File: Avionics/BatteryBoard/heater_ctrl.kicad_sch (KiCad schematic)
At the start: 0 parts

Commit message: Added heater control sub-schematic to battery board
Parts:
- added R13: 10k, symbol Device:R_US
- added R14: 31.6k, symbol Device:R_US
- added R15: 1.5k, symbol Device:R_US
- added U10: LMV331, symbol Comparator:LMV331
- added U11, U12: 74AHC1G08, symbol 74xGxx:74AHC1G08
- added U13: 74AHC1G32, symbol 74xGxx:74AHC1G32
- added U14: 74AHC1G04, symbol 74xGxx:74AHC1G04
- added U8: LM4040DBZ-2.5, Package_TO_SOT_SMD:SOT-23, symbol Reference_Voltage:LM4040DBZ-2.5
- added U9: TMP36xS, Package_SO:SOIC-8_3.9x4.9mm_P1.27mm, symbol Sensor_Temperature:TMP36xS
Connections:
- new net: U10.3 (-), U9.1 (V_{OUT})
- new net: R13.1, R14.2, U10.1 (+)
- new net: U12.1, U14.2
- new net: U11.2, U14.4
- new net: R14.1, R15.1, U8.1 (K)
- new net: U10.4, U11.1
- new net: U11.4, U13.1
- new net: U12.4, U13.2
- new net GNDREF: R13.2, U10.2 (V-), U11.3 (GND), U12.3 (GND), U13.3 (GND), U14.3 (GND), U8.2 (A), U9.4 (GND), U9.5 (~{SHUTDOWN})
- new net VCC: R15.2, U10.5 (V+), U11.5 (VCC), U12.5 (VCC), U13.5 (VCC), U14.5 (VCC), U9.8 (+Vs)

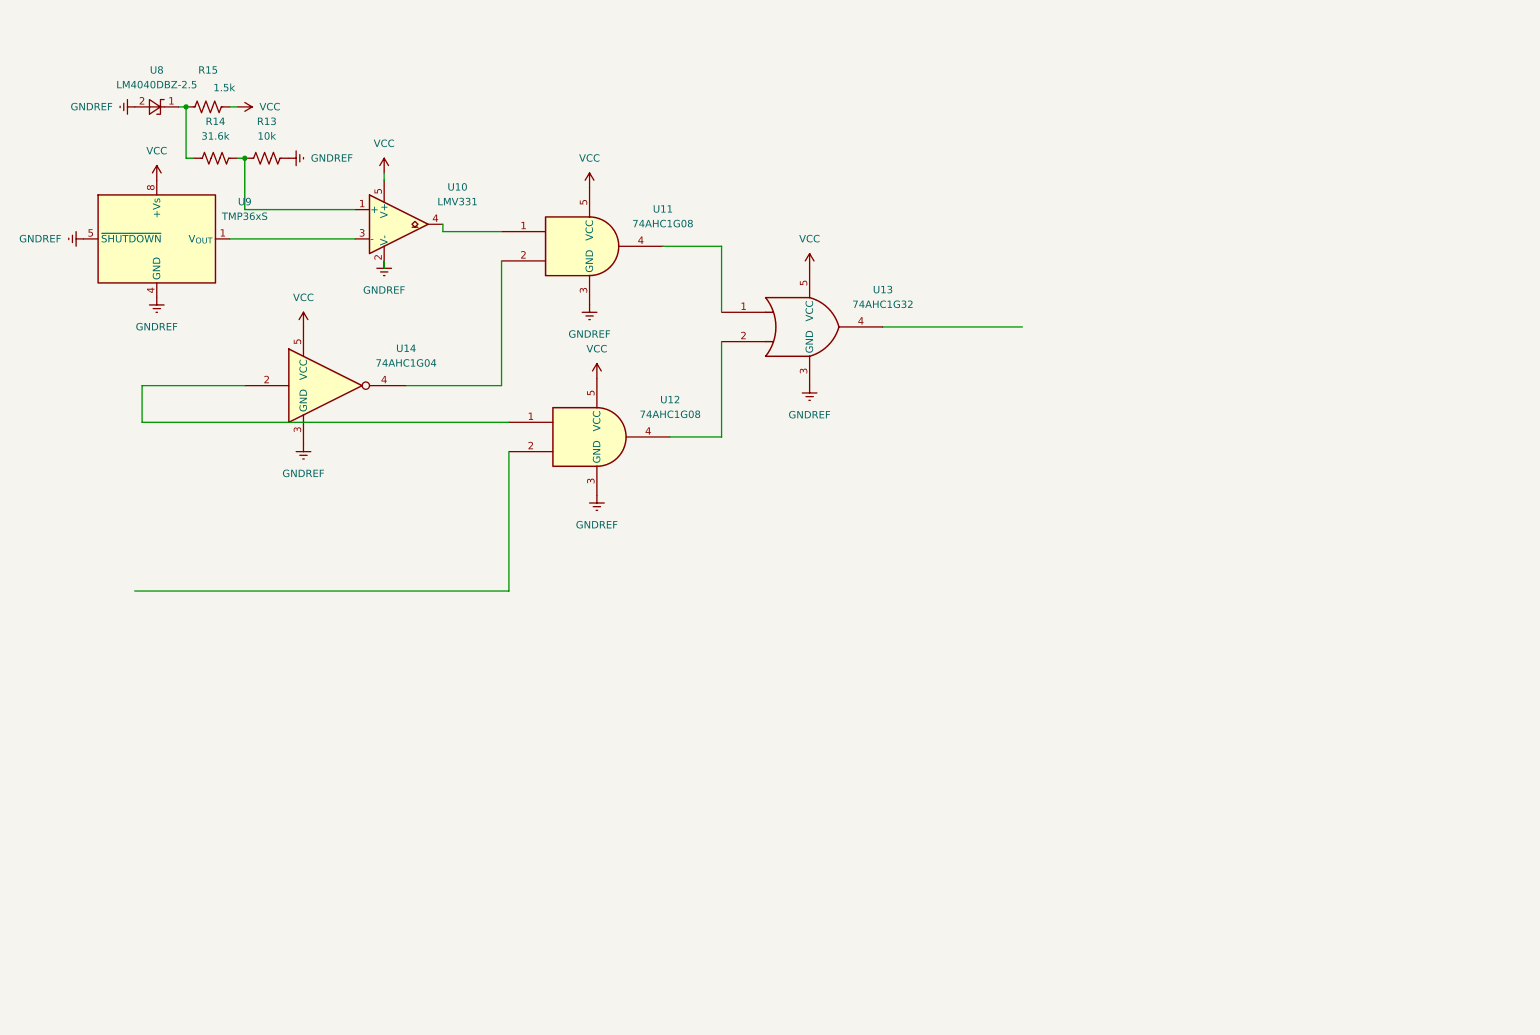
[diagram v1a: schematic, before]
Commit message: (5/18/25)(Ned Sigler) removed crossing wires
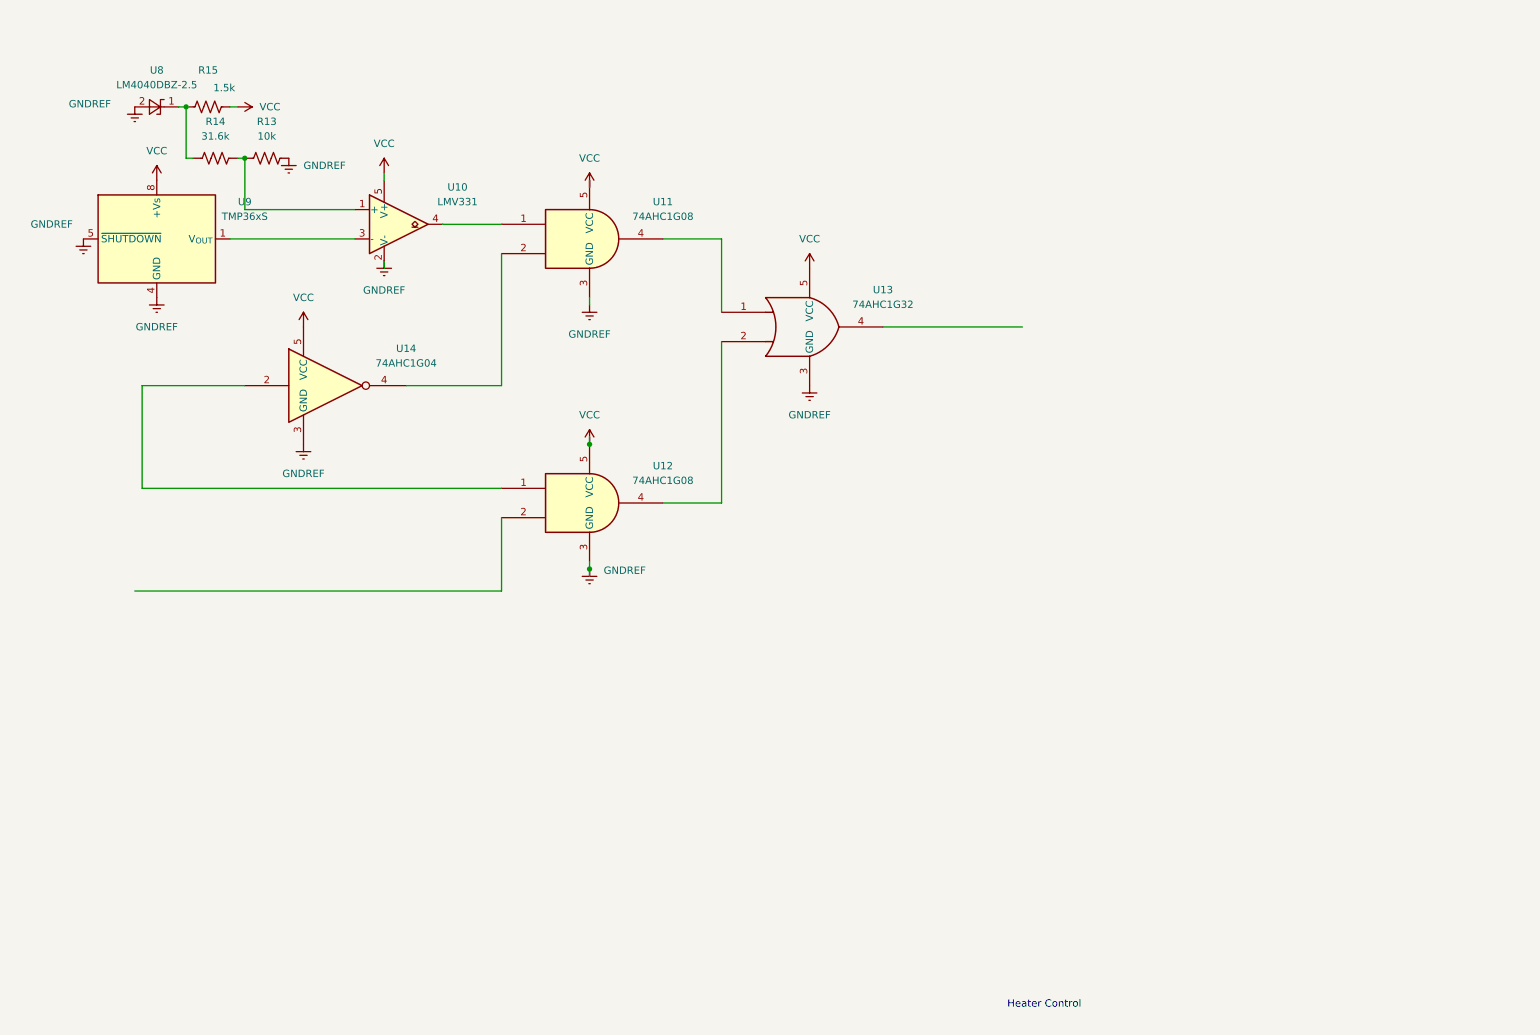
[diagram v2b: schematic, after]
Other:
- note added: "Heater Control"
- moved on the sheet: U11, U12

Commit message: batt_brd: discrete heater control has own 5v ldo
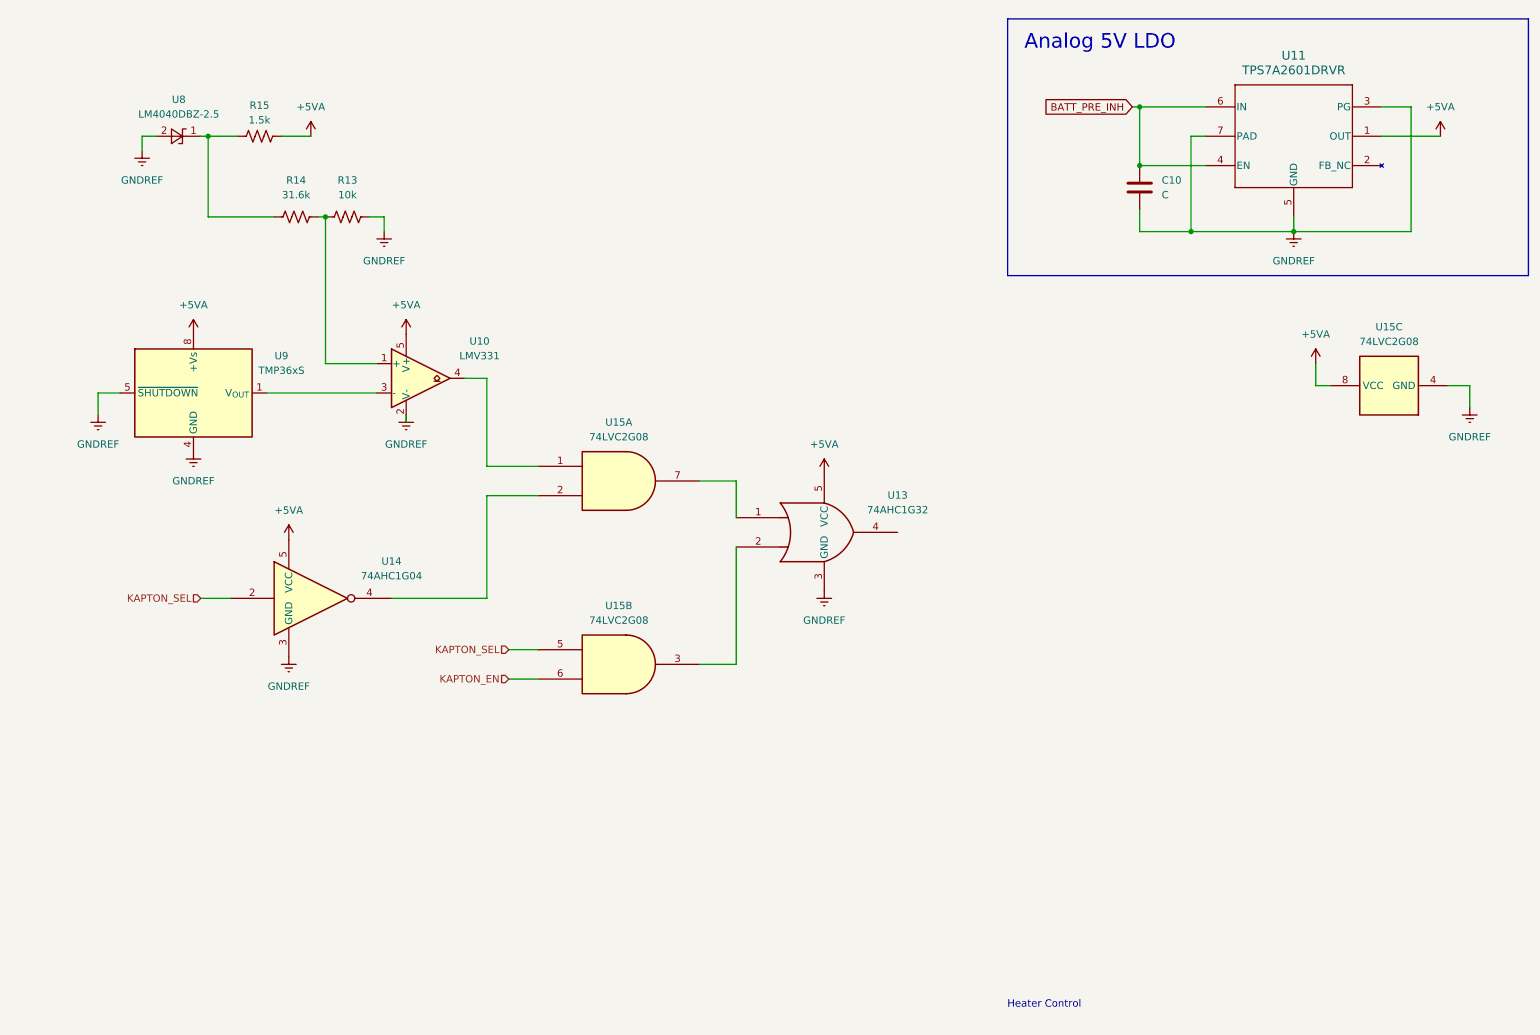
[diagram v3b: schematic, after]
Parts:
- removed U11, U12: 74AHC1G08, symbol 74xGxx:74AHC1G08
- added C10: C, symbol Device:C
- added U11: TPS7A2601DRVR, DRV0006A, symbol TPS7A2650DRVR:TPS7A2601DRVR
- added U15: 74LVC2G08, symbol 74xGxx:74LVC2G08
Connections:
- net GNDREF: now also C10.2, U11.3 (PG), U11.5 (GND), U11.7 (PAD), U15.4 (GND)
- net KAPTON_SEL: now reaches U14.2
- net KAPTON_SEL: now also U15.5
- net at U14.4: now also U15.2
- net at U10.4: now also U15.1
- net at U13.1: now also U15.7
- net at U13.2: now also U15.3
- net VCC renamed +5VA
- net +5VA: now also U11.1 (OUT), U15.8 (VCC)
- new net BATT_PRE_INH: C10.1, U11.4 (EN), U11.6 (IN)
- new net KAPTON_EN: U15.6
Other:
- note added: "Analog 5V LDO"
- moved on the sheet: R13, R14, R15, U10, U13, U14, U8, U9

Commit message: batt_brd: prettify
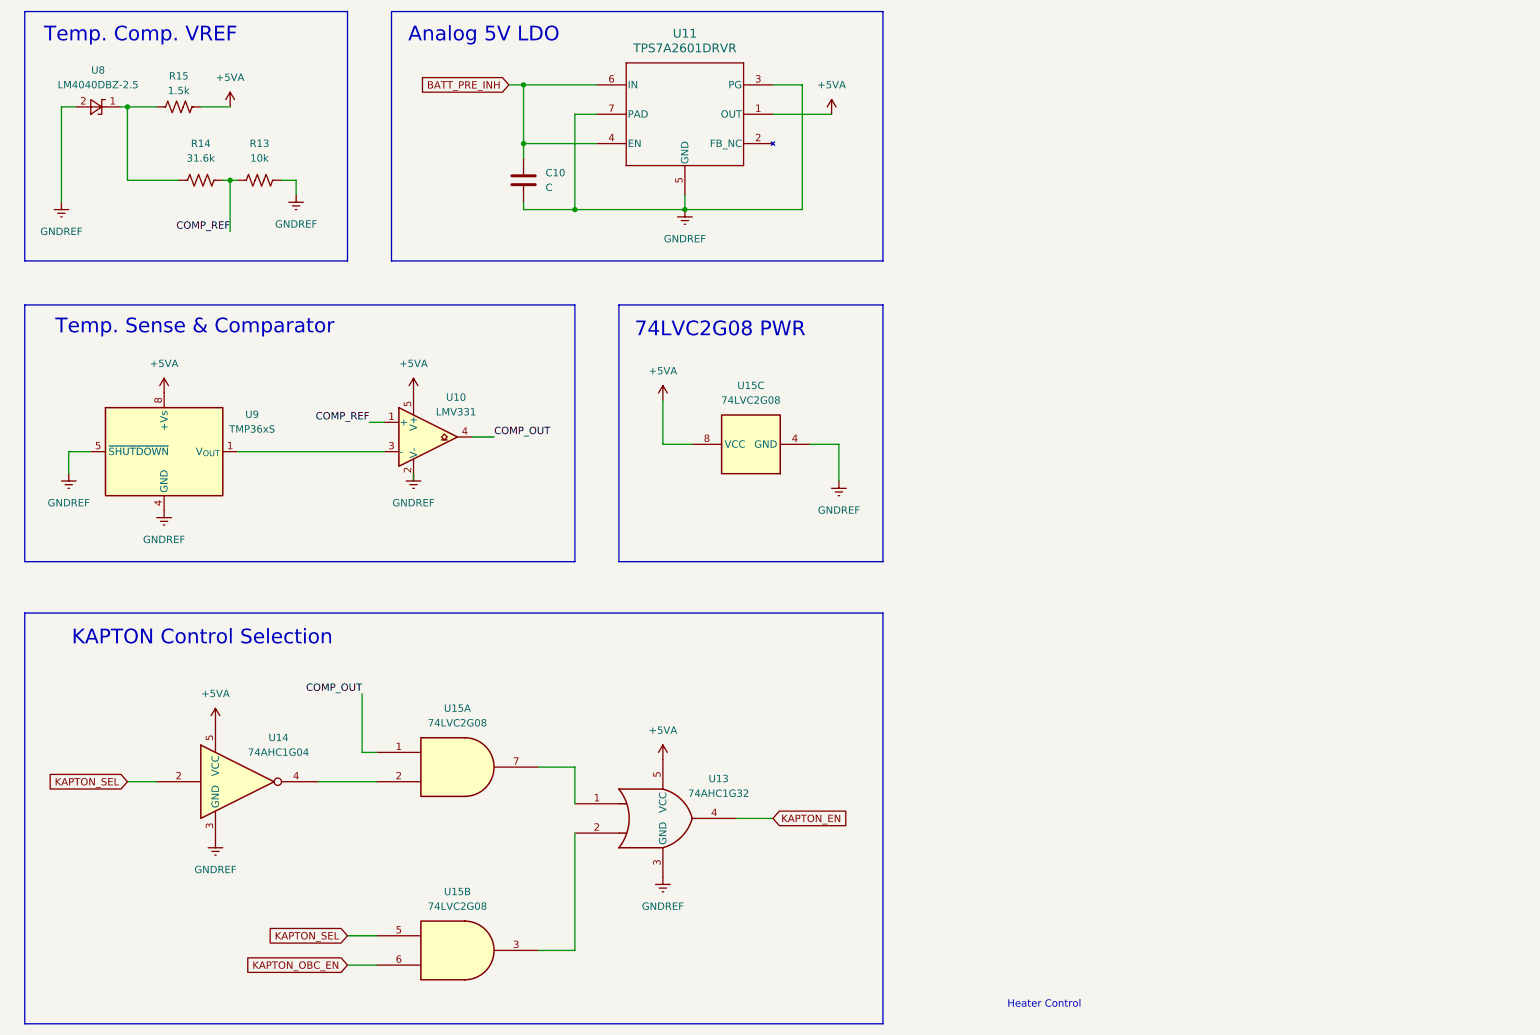
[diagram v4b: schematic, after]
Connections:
- net KAPTON_EN: now also U13.4; no longer U15.6
- net COMP_REF: now reaches R13.1, R14.2, U10.1 (+)
- net COMP_OUT: now reaches U10.4, U15.1
- new net KAPTON_OBC_EN: U15.6
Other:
- note added: "74LVC2G08 PWR"
- note added: "KAPTON Control Selection"
- note added: "Temp. Comp. VREF"
- note added: "Temp. Sense & Comparator"
- moved on the sheet: C10, R13, R14, R15, U10, U11, U13, U14, U15A, U15B, U15C, U8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

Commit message: batt_brd: add decoupling caps & fix comparator output
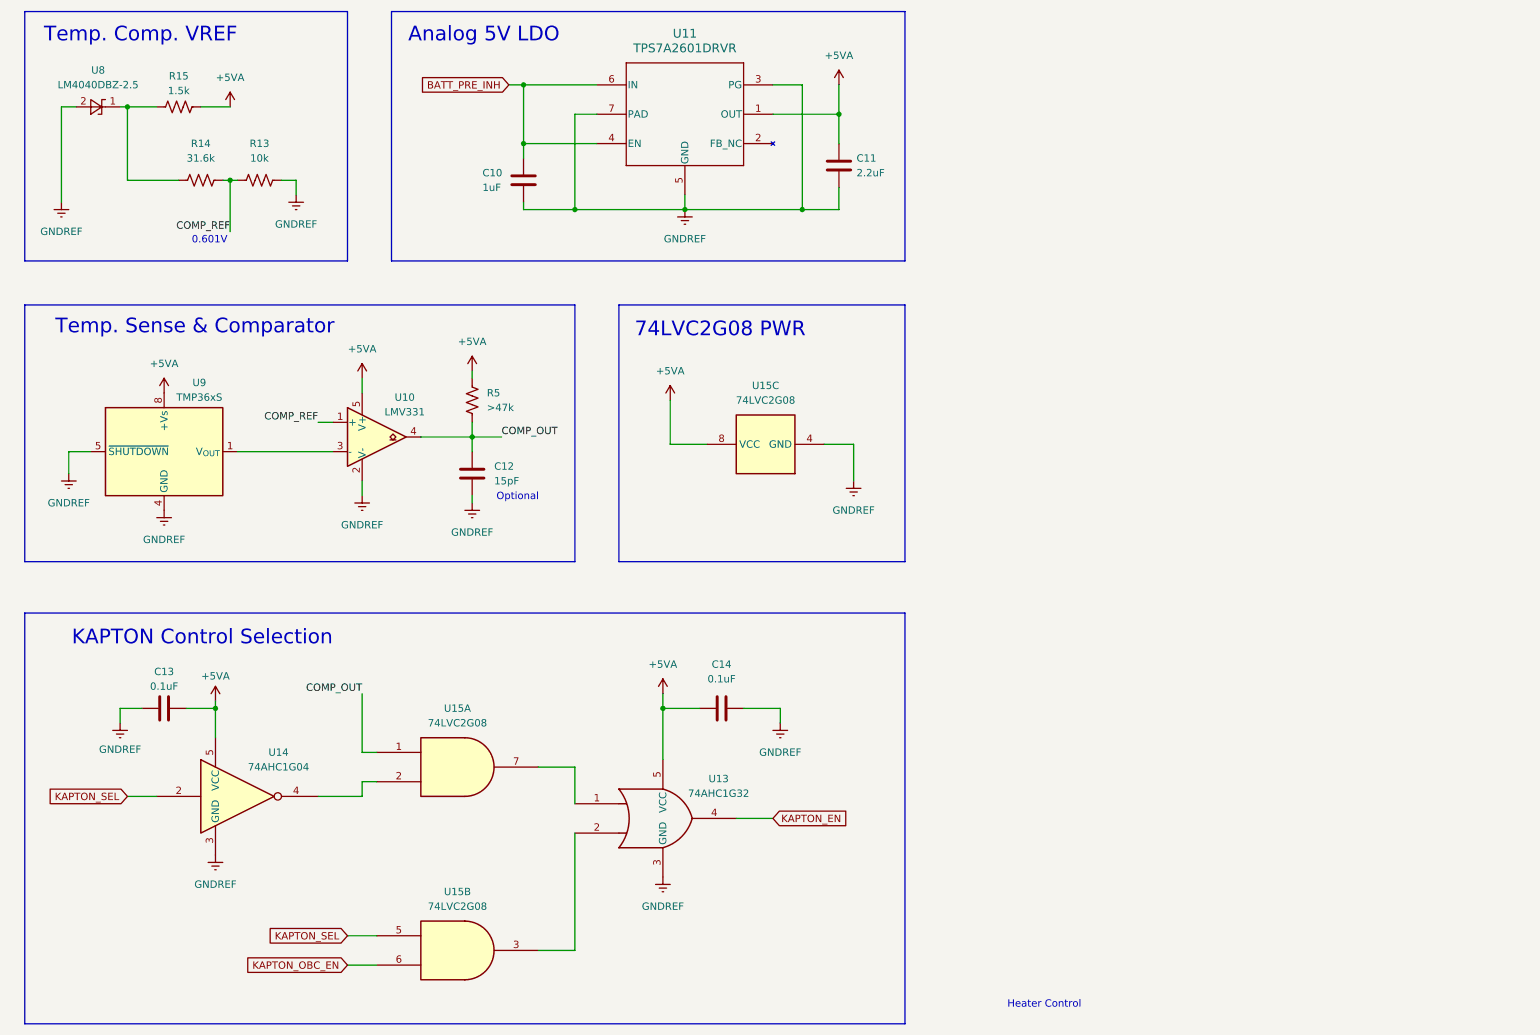
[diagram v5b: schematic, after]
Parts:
- added C11: 2.2uF, symbol Device:C
- added C12: 15pF, symbol Device:C
- added C13, C14: 0.1uF, symbol Device:C
- added R5: >47k, symbol Device:R_US
- C10: value C -> 1uF
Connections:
- net +5VA: now also C11.1, C13.2, C14.1, R5.1
- net COMP_OUT: now also C12.1, R5.2
- net GNDREF: now also C11.2, C12.2, C13.1, C14.2
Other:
- note added: "0.601V"
- note added: "Optional"
- moved on the sheet: U10, U14, U15C

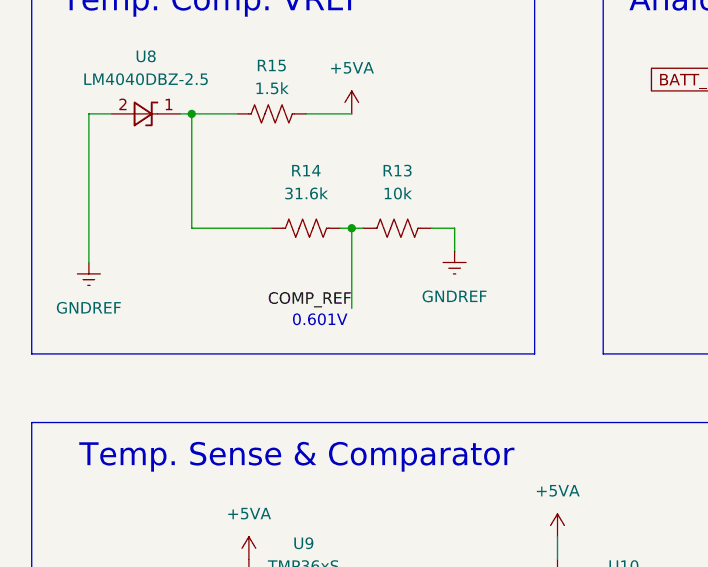
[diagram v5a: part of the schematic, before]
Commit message: batt_brd: more labels
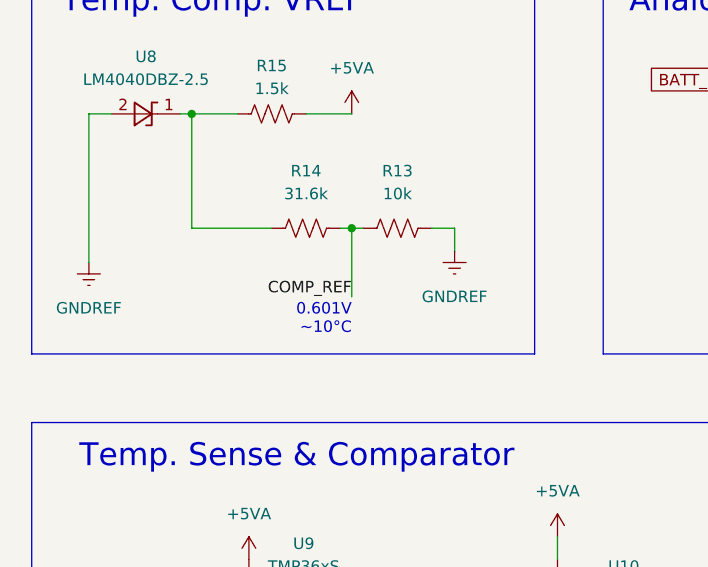
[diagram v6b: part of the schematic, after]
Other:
- note added: "0.601V ~10°C"
- note removed: "0.601V"
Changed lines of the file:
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@@
 		)
 	)
-	(text "0.601V"
+	(text "0.601V\n~10°C"
 		(exclude_from_sim no)
-		(at 49.784 57.404 0)
+		(at 53.34 57.15 0)
 		(effects
 			(font
 				(size 1.27 1.27)
 			)
+			(justify right)
 		)
 	)
@@
 	(wire
 		(pts
-			(xy 53.34 46.99) (xy 53.34 55.88)
+			(xy 53.34 46.99) (xy 53.34 54.61)
 		)
 		(stroke
@@
 	)
 	(label "COMP_REF"
-		(at 53.34 55.88 180)
+		(at 53.34 54.61 180)
 		(effects
 			(font
